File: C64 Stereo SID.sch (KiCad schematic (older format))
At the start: 16 parts, among them J1 EXT_IN_SEL1, J2 EXT_IN_SEL2, J3 AUD_OUT2, J4 ~CS, Q1 2N2222, U1 MOS_6581, U2 MOS_6581

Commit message: Assigned footprints
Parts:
- A1: footprint (none) -> MOS_6581:MOS_6581_Adapter
- C70, C71, C74, C76: footprint (none) -> Capacitors_THT:C_Disc_D4.7mm_W2.5mm_P5.00mm
- C77: footprint (none) -> Capacitors_THT:CP_Radial_D4.0mm_P2.00mm
- J1, J2: footprint (none) -> Pin_Headers:Pin_Header_Straight_1x03_Pitch2.54mm
- J3: footprint (none) -> Pin_Headers:Pin_Header_Straight_1x02_Pitch2.54mm
- J4: footprint (none) -> Pin_Headers:Pin_Header_Straight_1x01_Pitch2.54mm
- R12, R8, R9: footprint (none) -> Resistors_THT:R_Axial_DIN0207_L6.3mm_D2.5mm_P10.16mm_Horizontal
- U1, U2: footprint (none) -> Housings_DIP:DIP-28_W15.24mm_Socket
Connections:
- net labels removed: AUD_OUT2
- wire segments 115 -> 114
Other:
- note added: "SID #1"
- note added: "SID #2"
- moved on the sheet: A1, C70, C71, C74, C76, C77, J1, J2, J3, Q1, R12, R8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

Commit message: Tracks routed and silkscreen added
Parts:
- removed J4: ~CS, Pin_Headers:Pin_Header_Straight_1x01_Pitch2.54mm, symbol Conn_01x01
- added J4: ~CS, Pin_Headers:Pin_Header_Straight_1x02_Pitch2.54mm, symbol Conn_01x02
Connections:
- wire segments 114 -> 116
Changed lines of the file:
@@
 NoConn ~ 6225 1625
 NoConn ~ 6225 1725
-Text GLabel 4600 1925 0    60   Output ~ 0
+Text GLabel 4600 1925 0    60   Input ~ 0
 ~CS2
 Text Label 6250 5100 0    60   ~ 0
@@
 U 1 1 5D19785E
 P 4600 1150
-F 0 "C71" V 4650 1200 50  0000 L CNN
-F 1 "470pF" V 4750 1150 50  0000 C CNN
+F 0 "C71" V 4700 1150 50  0000 C CNN
+F 1 "470pF" V 4500 1150 50  0000 C CNN
 F 2 "Capacitors_THT:C_Disc_D4.7mm_W2.5mm_P5.00mm" H 4600 1150 50  0001 C CNN
 F 3 "" H 4600 1150 50  0001 C CNN
 	1    4600 1150
-	0    -1   -1   0
+	0    1    1    0
 $EndComp
 $Comp
@@
 U 1 1 5D1979D4
 P 4350 1150
-F 0 "C70" V 4400 1200 50  0000 L CNN
-F 1 "470pF" V 4500 1150 50  0000 C CNN
+F 0 "C70" V 4450 1150 50  0000 C CNN
+F 1 "470pF" V 4250 1150 50  0000 C CNN
 F 2 "Capacitors_THT:C_Disc_D4.7mm_W2.5mm_P5.00mm" H 4350 1150 50  0001 C CNN
 F 3 "" H 4350 1150 50  0001 C CNN
 	1    4350 1150
-	0    -1   -1   0
+	0    1    1    0
 $EndComp
 $Comp
@@
 	1    0    0    -1
 $EndComp
-$Comp
-L Conn_01x01 J4
-U 1 1 5D19887E
-P 4975 3050
-F 0 "J4" H 4975 3150 50  0000 C CNN
-F 1 "~CS" H 4975 2950 50  0000 C CNN
-F 2 "Pin_Headers:Pin_Header_Straight_1x01_Pitch2.54mm" H 4975 3050 50  0001 C CNN
-F 3 "" H 4975 3050 50  0001 C CNN
-	1    4975 3050
-	1    0    0    -1
-$EndComp
-Text GLabel 4700 3050 0    60   Input ~ 0
+Text GLabel 4750 3050 0    60   Output ~ 0
 ~CS2
 $Comp
@@
 U 1 1 5D19A9A8
 P 7875 2025
-F 0 "C76" H 7725 1950 50  0000 L CNN
-F 1 "470pF" V 7975 2025 50  0000 C CNN
+F 0 "C76" H 7900 2100 50  0000 L CNN
+F 1 "470pF" V 7750 2025 50  0000 C CNN
 F 2 "Capacitors_THT:C_Disc_D4.7mm_W2.5mm_P5.00mm" H 7875 2025 50  0001 C CNN
 F 3 "" H 7875 2025 50  0001 C CNN
 	1    7875 2025
-	1    0    0    -1
+	-1   0    0    1
 $EndComp
 $Comp
@@
 	8875 2300 8875 2375
 Wire Wire Line
-	4700 3050 4775 3050
+	4750 3050 4825 3050
 Wire Wire Line
 	6225 1325 7875 1325
@@
 Text Notes 5350 5800 0    60   ~ 0
 SID #1
+$Comp
+L VCC #PWR017
+U 1 1 5D1ADB09
+P 4425 3075
+F 0 "#PWR017" H 4425 2925 50  0001 C CNN
+F 1 "VCC" H 4425 3225 50  0000 C CNN
+F 2 "" H 4425 3075 50  0001 C CNN
+F 3 "" H 4425 3075 50  0001 C CNN
+	1    4425 3075
+	1    0    0    -1
+$EndComp
+Wire Wire Line
+	4425 3075 4425 3150
+Wire Wire Line
+	4425 3150 4825 3150
+$Comp
+L Conn_01x02 J4
+U 1 1 5D1ADE1F
+P 5025 3050
+F 0 "J4" H 5025 3150 50  0000 C CNN
+F 1 "~CS" H 5025 2850 50  0000 C CNN
+F 2 "Pin_Headers:Pin_Header_Straight_1x02_Pitch2.54mm" H 5025 3050 50  0001 C CNN
+F 3 "" H 5025 3050 50  0001 C CNN
+	1    5025 3050
+	1    0    0    -1
+$EndComp
 $EndSCHEMATC

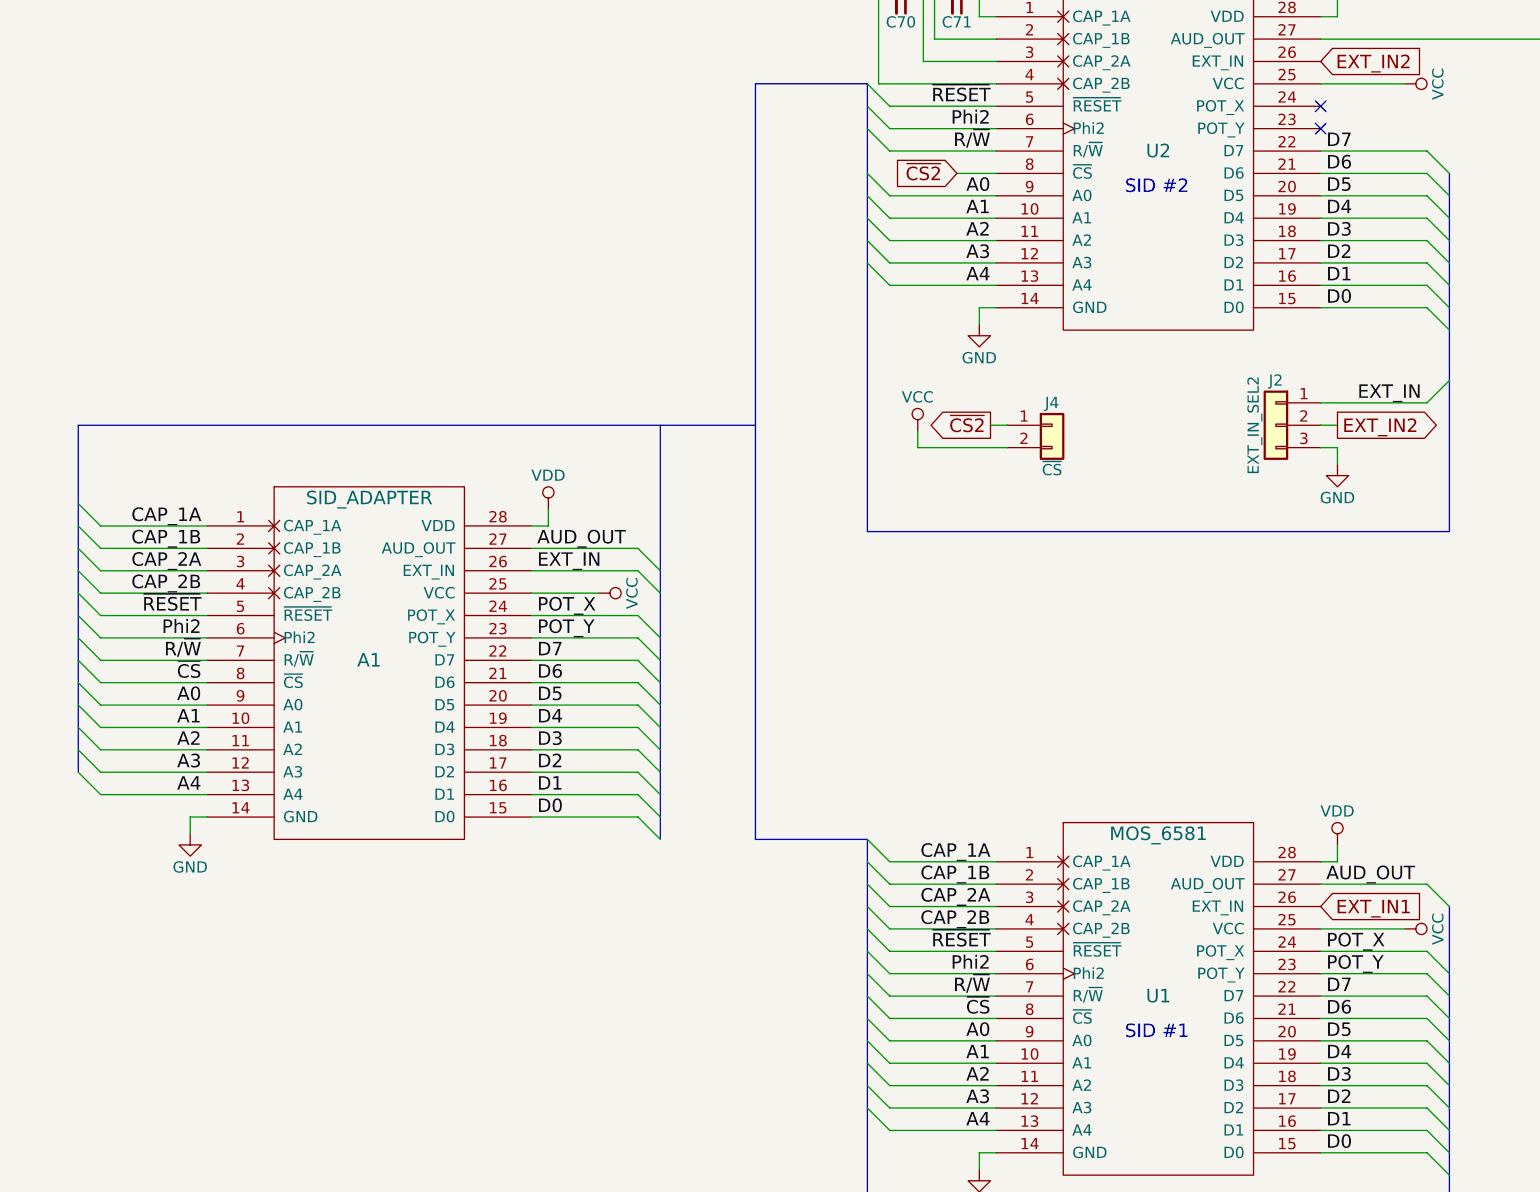
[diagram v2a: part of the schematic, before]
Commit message: Added header for swapping SIDs around
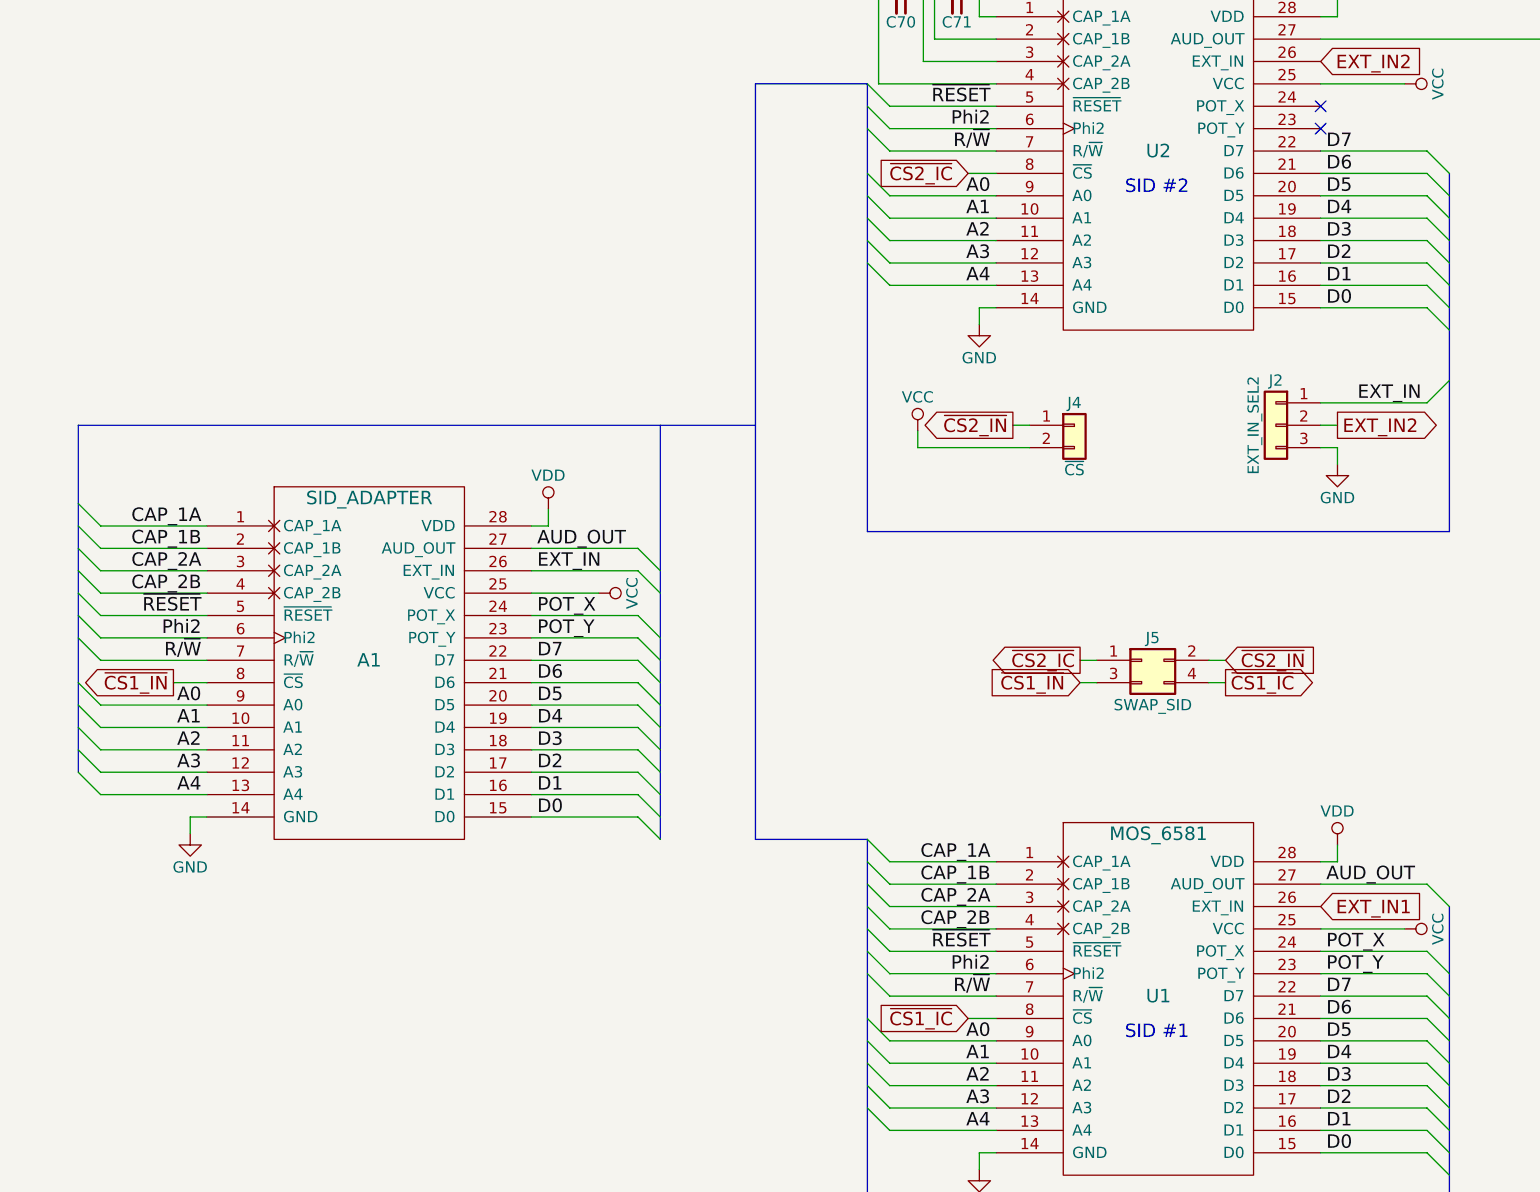
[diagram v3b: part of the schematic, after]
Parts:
- added J5: SWAP_SID, Pin_Headers:Pin_Header_Straight_2x02_Pitch2.54mm, symbol Conn_02x02_Odd_Even
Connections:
- net ~CS renamed ~CS1_IC
- net ~CS1_IC: now also J5.4 (Pin_4); no longer A1.8 (~CS)
- net ~CS2 renamed ~CS2_IC
- net ~CS2_IC: now also J5.1 (Pin_1); no longer J4.1 (Pin_1)
- new net ~CS1_IN: A1.8 (~CS), J5.3 (Pin_3)
- new net ~CS2_IN: J4.1 (Pin_1), J5.2 (Pin_2)
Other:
- moved on the sheet: J4
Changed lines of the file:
@@
 Text Label 1225 4100 2    60   ~ 0
 R/~W
-Text Label 1225 4200 2    60   ~ 0
-~CS
 Text Label 1225 4300 2    60   ~ 0
 A0
@@
 Entry Wire Line
 	775  4300 675  4200
-Entry Wire Line
-	775  4200 675  4100
 Entry Wire Line
 	775  4100 675  4000
@@
 Text Label 4750 5600 2    60   ~ 0
 R/~W
-Text Label 4750 5700 2    60   ~ 0
-~CS
 Text Label 4750 5800 2    60   ~ 0
 A0
@@
 Entry Wire Line
 	4300 5800 4200 5700
-Entry Wire Line
-	4300 5700 4200 5600
 Entry Wire Line
 	4300 5600 4200 5500
@@
 NoConn ~ 6225 1625
 NoConn ~ 6225 1725
-Text GLabel 4600 1925 0    60   Input ~ 0
-~CS2
+Text GLabel 4650 1925 0    60   Input ~ 0
+~CS2_IC
 Text Label 6250 5100 0    60   ~ 0
 AUD_OUT
@@
 	1    0    0    -1
 $EndComp
-Text GLabel 4750 3050 0    60   Output ~ 0
-~CS2
+Text GLabel 4850 3050 0    60   Output ~ 0
+~CS2_IN
 $Comp
 L R R8
@@
 	1250 4100 775  4100
 Wire Wire Line
-	1250 4200 775  4200
-Wire Wire Line
 	1250 4300 775  4300
 Wire Wire Line
@@
 Wire Wire Line
 	4775 5600 4300 5600
-Wire Wire Line
-	4775 5700 4300 5700
 Wire Wire Line
 	4775 5800 4300 5800
@@
 	6800 1925 6800 3525
 Wire Wire Line
-	4600 1925 4775 1925
-Wire Wire Line
 	4700 1150 4700 1225
 Wire Wire Line
@@
 	8875 2300 8875 2375
 Wire Wire Line
-	4750 3050 4825 3050
+	4850 3050 4925 3050
 Wire Wire Line
 	6225 1325 7875 1325
@@
 	4425 3075 4425 3150
 Wire Wire Line
-	4425 3150 4825 3150
+	4425 3150 4925 3150
 $Comp
 L Conn_01x02 J4
 U 1 1 5D1ADE1F
-P 5025 3050
-F 0 "J4" H 5025 3150 50  0000 C CNN
-F 1 "~CS" H 5025 2850 50  0000 C CNN
-F 2 "Pin_Headers:Pin_Header_Straight_1x02_Pitch2.54mm" H 5025 3050 50  0001 C CNN
-F 3 "" H 5025 3050 50  0001 C CNN
-	1    5025 3050
-	1    0    0    -1
-$EndComp
+P 5125 3050
+F 0 "J4" H 5125 3150 50  0000 C CNN
+F 1 "~CS" H 5125 2850 50  0000 C CNN
+F 2 "Pin_Headers:Pin_Header_Straight_1x02_Pitch2.54mm" H 5125 3050 50  0001 C CNN
+F 3 "" H 5125 3050 50  0001 C CNN
+	1    5125 3050
+	1    0    0    -1
+$EndComp
+Text GLabel 1100 4200 0    60   Output ~ 0
+~CS1_IN
+$Comp
+L Conn_02x02_Odd_Even J5
+U 1 1 5D1A537A
+P 5425 4100
+F 0 "J5" H 5475 4200 50  0000 C CNN
+F 1 "SWAP_SID" H 5475 3900 50  0000 C CNN
+F 2 "Pin_Headers:Pin_Header_Straight_2x02_Pitch2.54mm" H 5425 4100 50  0001 C CNN
+F 3 "" H 5425 4100 50  0001 C CNN
+	1    5425 4100
+	1    0    0    -1
+$EndComp
+Wire Wire Line
+	4650 1925 4775 1925
+Text GLabel 4650 5700 0    60   Input ~ 0
+~CS1_IC
+Wire Wire Line
+	4650 5700 4775 5700
+Wire Wire Line
+	1100 4200 1250 4200
+Text GLabel 5150 4100 0    60   Output ~ 0
+~CS2_IC
+Text GLabel 5800 4200 2    60   Output ~ 0
+~CS1_IC
+Text GLabel 5800 4100 2    60   Input ~ 0
+~CS2_IN
+Text GLabel 5150 4200 0    60   Input ~ 0
+~CS1_IN
+Wire Wire Line
+	5150 4100 5225 4100
+Wire Wire Line
+	5150 4200 5225 4200
+Wire Wire Line
+	5725 4100 5800 4100
+Wire Wire Line
+	5725 4200 5800 4200
 $EndSCHEMATC

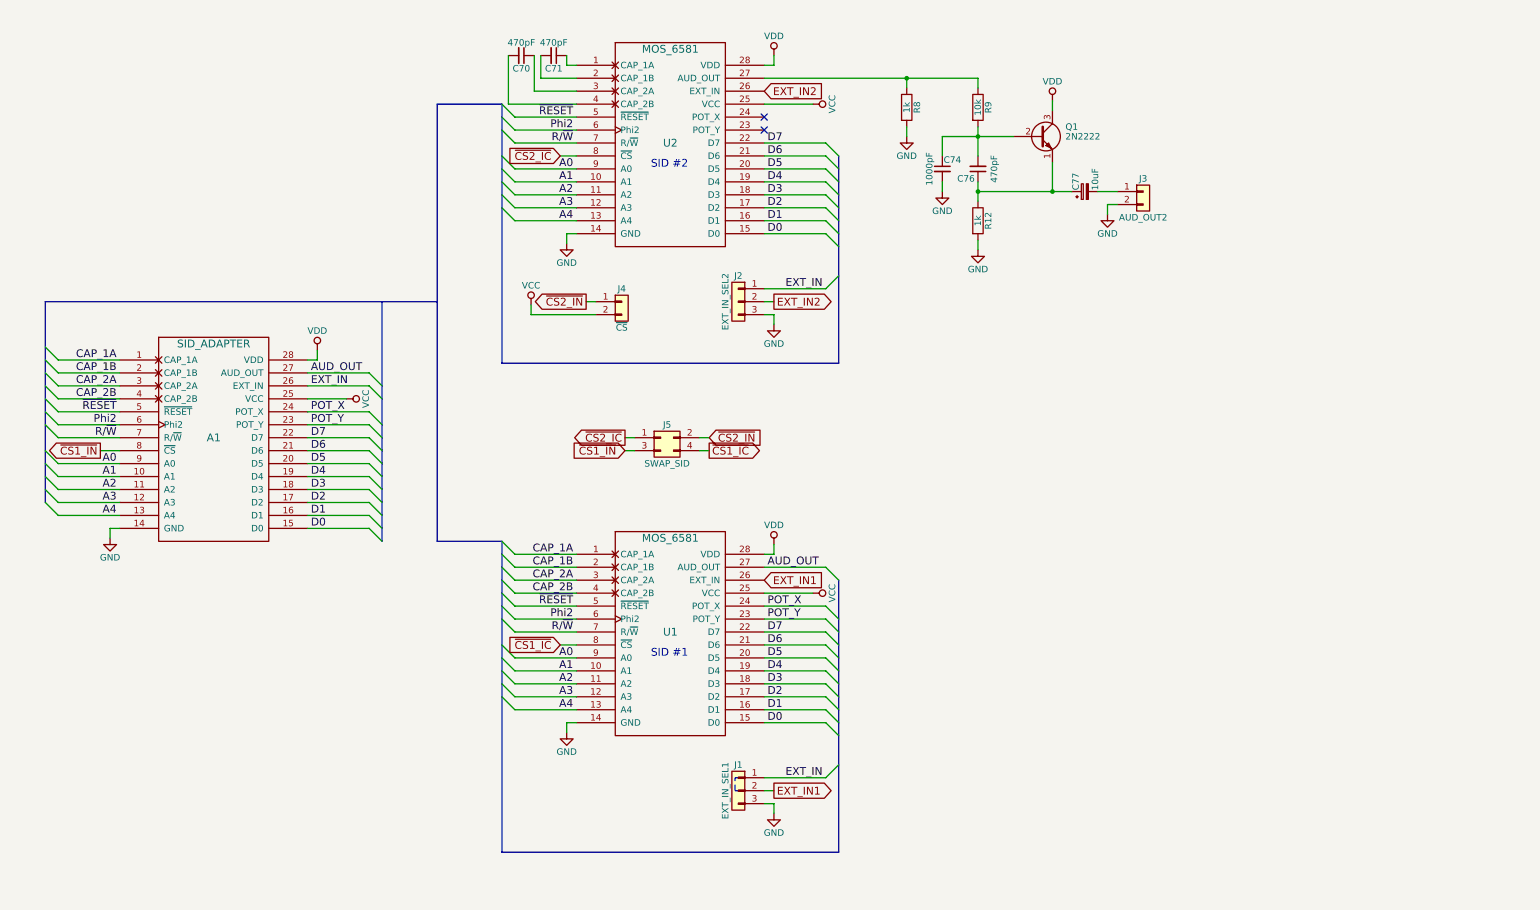
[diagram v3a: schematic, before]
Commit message: Changed to select SIDs as pseudo stereo
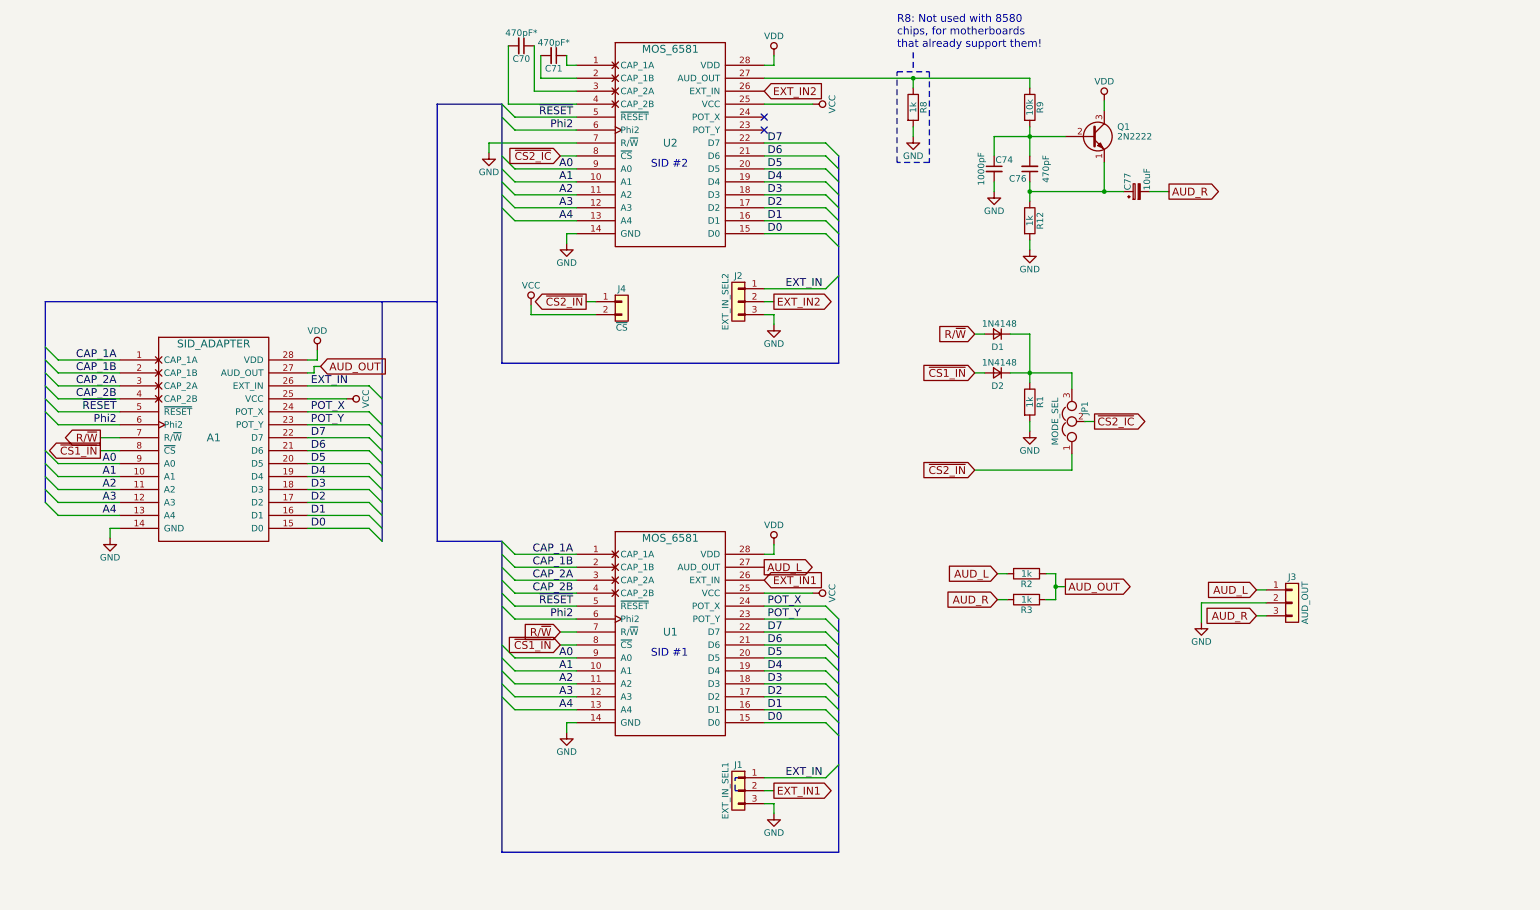
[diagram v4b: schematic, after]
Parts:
- removed J3: AUD_OUT2, Pin_Headers:Pin_Header_Straight_1x02_Pitch2.54mm, symbol Conn_01x02
- removed J5: SWAP_SID, Pin_Headers:Pin_Header_Straight_2x02_Pitch2.54mm, symbol Conn_02x02_Odd_Even
- added D1, D2: 1N4148, Diodes_THT:D_DO-35_SOD27_P7.62mm_Horizontal, symbol D_Small
- added J3: AUD_OUT, Pin_Headers:Pin_Header_Straight_1x03_Pitch2.54mm, symbol Conn_01x03
- added JP1: MODE_SEL, Pin_Headers:Pin_Header_Straight_1x03_Pitch2.54mm, symbol Jumper_NC_Dual
- added R1, R2, R3: 1k, Resistors_THT:R_Axial_DIN0207_L6.3mm_D2.5mm_P10.16mm_Horizontal, symbol R
- C70, C71: value 470pF -> 470pF*
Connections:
- net ~CS1_IC is gone; now on net ~CS1_IN: U1.8 (~CS)
- net AUD_OUT: now also R2.1, R3.1; no longer U1.27 (AUD_OUT)
- net GND: now also U2.7 (R/~W), J3.2 (Pin_2), R1.2
- net R/~W: now also D1.2 (A); no longer U2.7 (R/~W)
- net ~CS1_IN: now also D2.2 (A)
- net ~CS2_IC: now also JP1.2
- net ~CS2_IN: now also JP1.1
- net AUD_R: now reaches C77.2
- net AUD_R: now also J3.3 (Pin_3), R3.2
- new net: D1.1 (K), D2.1 (K), JP1.3, R1.1
- new net AUD_L: J3.1 (Pin_1), R2.2, U1.27 (AUD_OUT)
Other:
- note added: "R8: Not used with 8580\nchips, for motherboards\nthat already support them!"
- moved on the sheet: C70, C74, C76, C77, Q1, R12, R8, R9
